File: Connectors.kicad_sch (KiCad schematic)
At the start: 27 parts

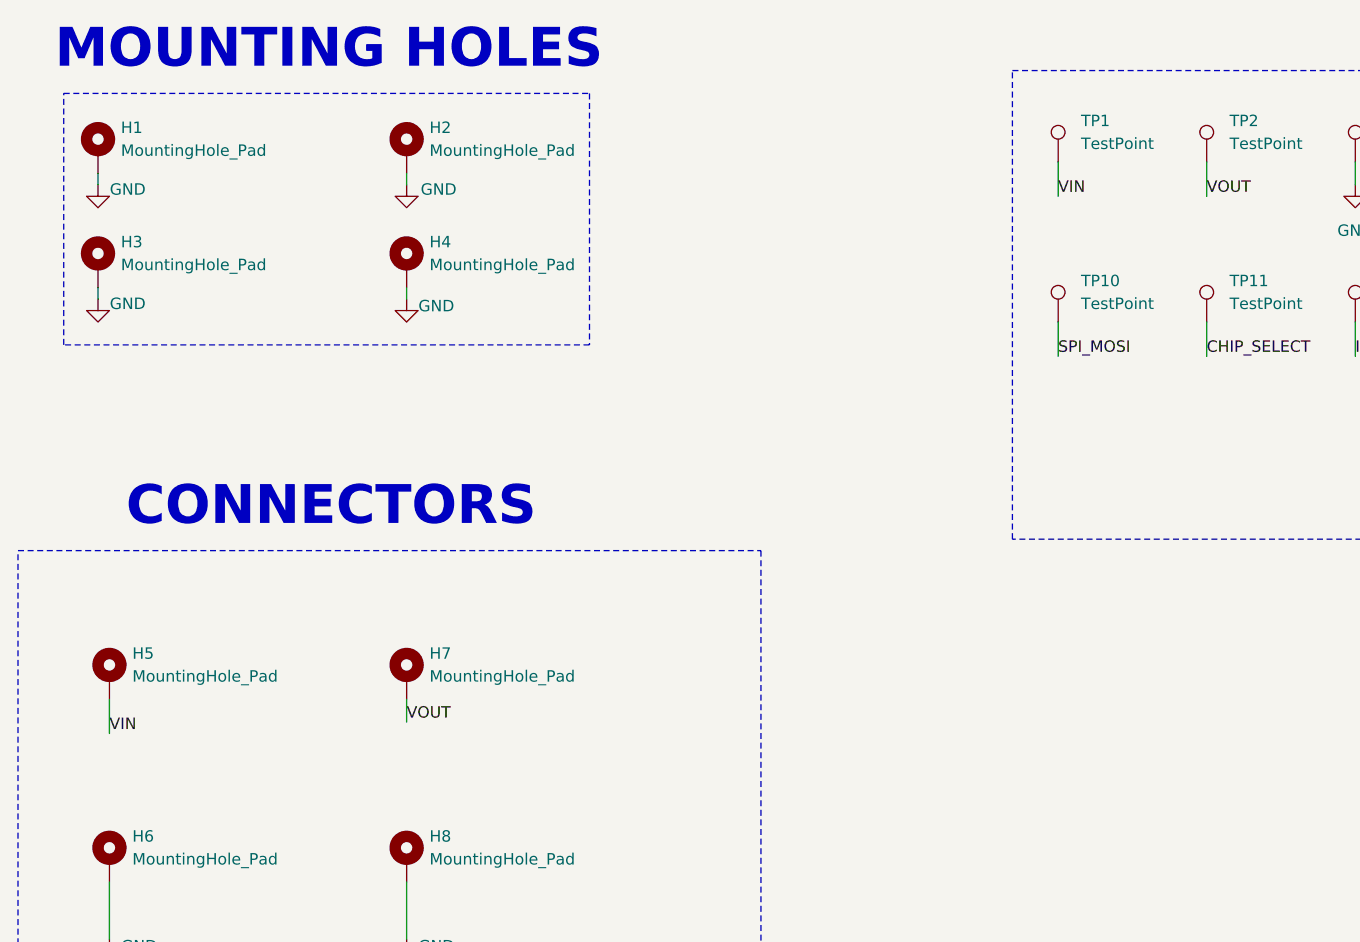
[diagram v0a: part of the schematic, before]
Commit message: Commercial components selected
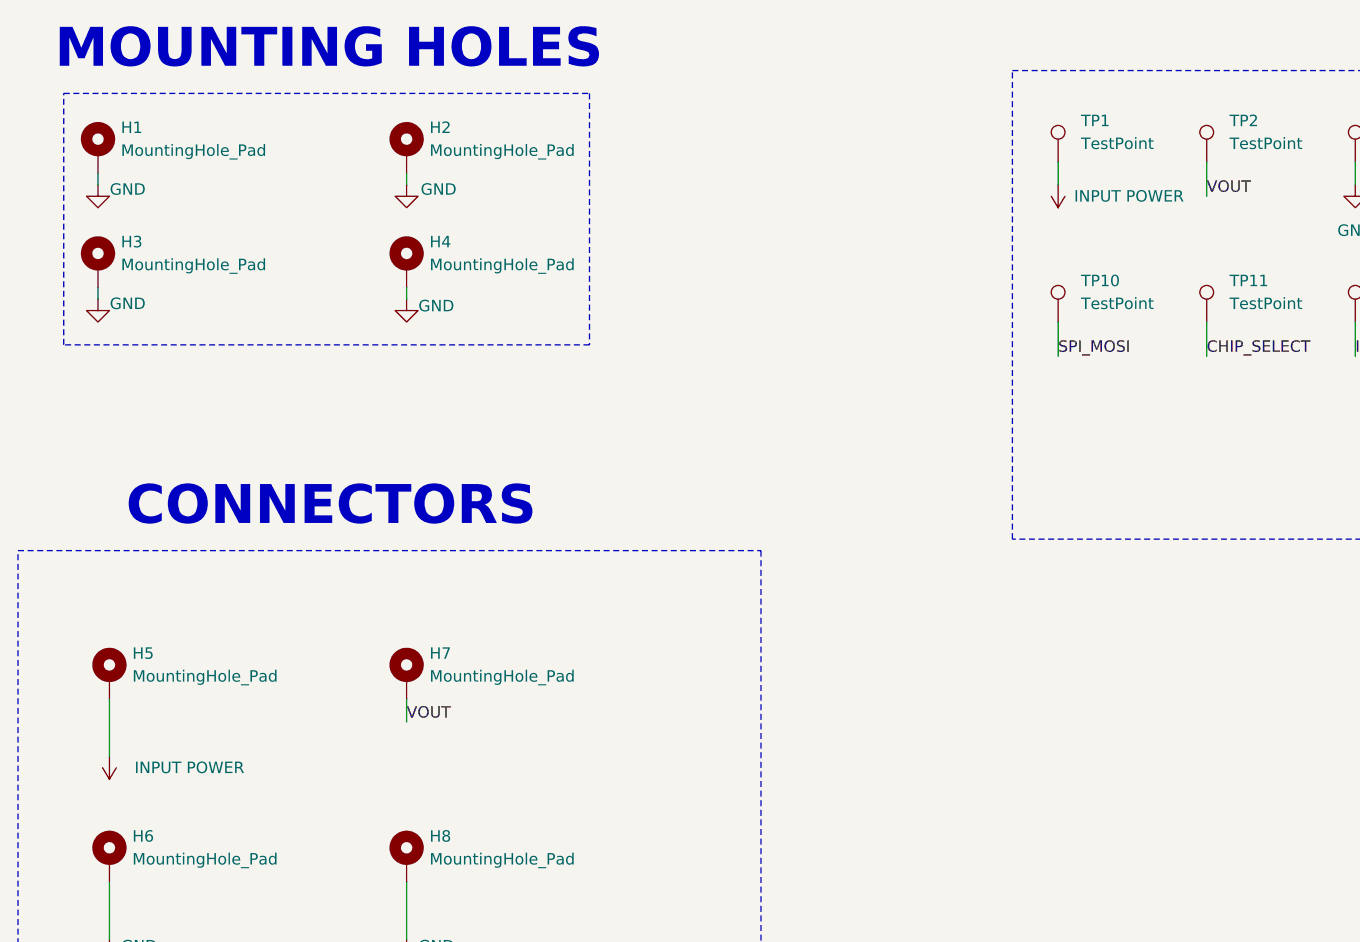
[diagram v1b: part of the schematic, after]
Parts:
- TP1, TP10, TP11, TP12, TP13, TP14, TP15, TP2, TP3, TP4, TP5, TP6, TP7, TP8, TP9: footprint TestPoint:TestPoint_Loop_D2.54mm_Drill1.5mm_Beaded -> TestPoint:TestPoint_Loop_D2.50mm_Drill1.0mm; Distributor Link (none) -> https://www.digikey.es/es/products/detail/keystone-electron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
- TP16, TP17, TP18, TP19: Distributor Link (none) -> https://www.digikey.es/es/products/detail/keystone-electron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
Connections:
- net VIN is gone; now on net INPUT POWER: H5.1, TP1.1
